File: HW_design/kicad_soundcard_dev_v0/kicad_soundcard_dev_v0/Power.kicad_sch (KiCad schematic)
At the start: 18 parts, among them J101 USB_C_Receptacle_USB2.0_16P, U101 AMS1117-3.3, U102 AMS1117-3.3

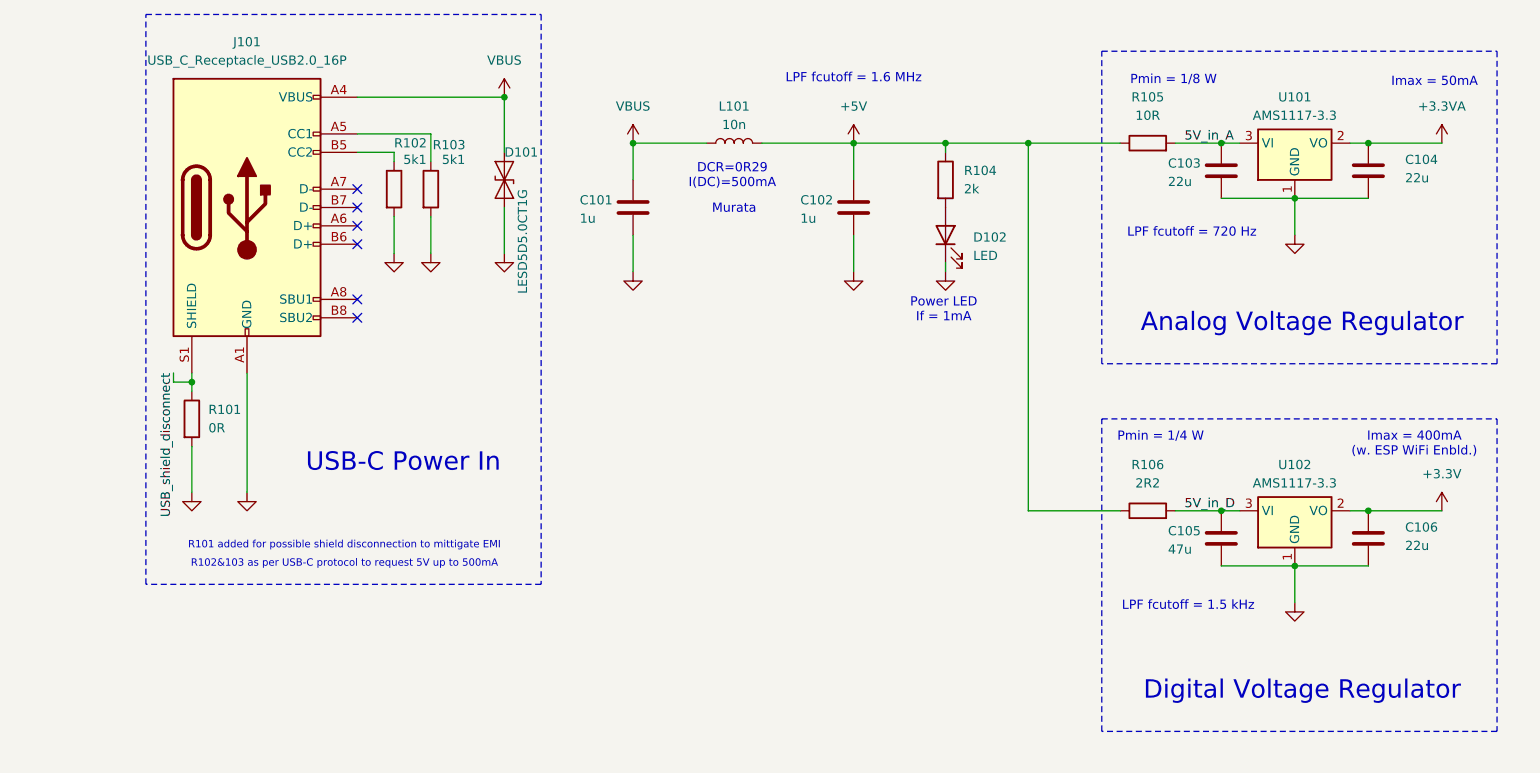
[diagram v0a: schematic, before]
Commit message: Changed Directory structure
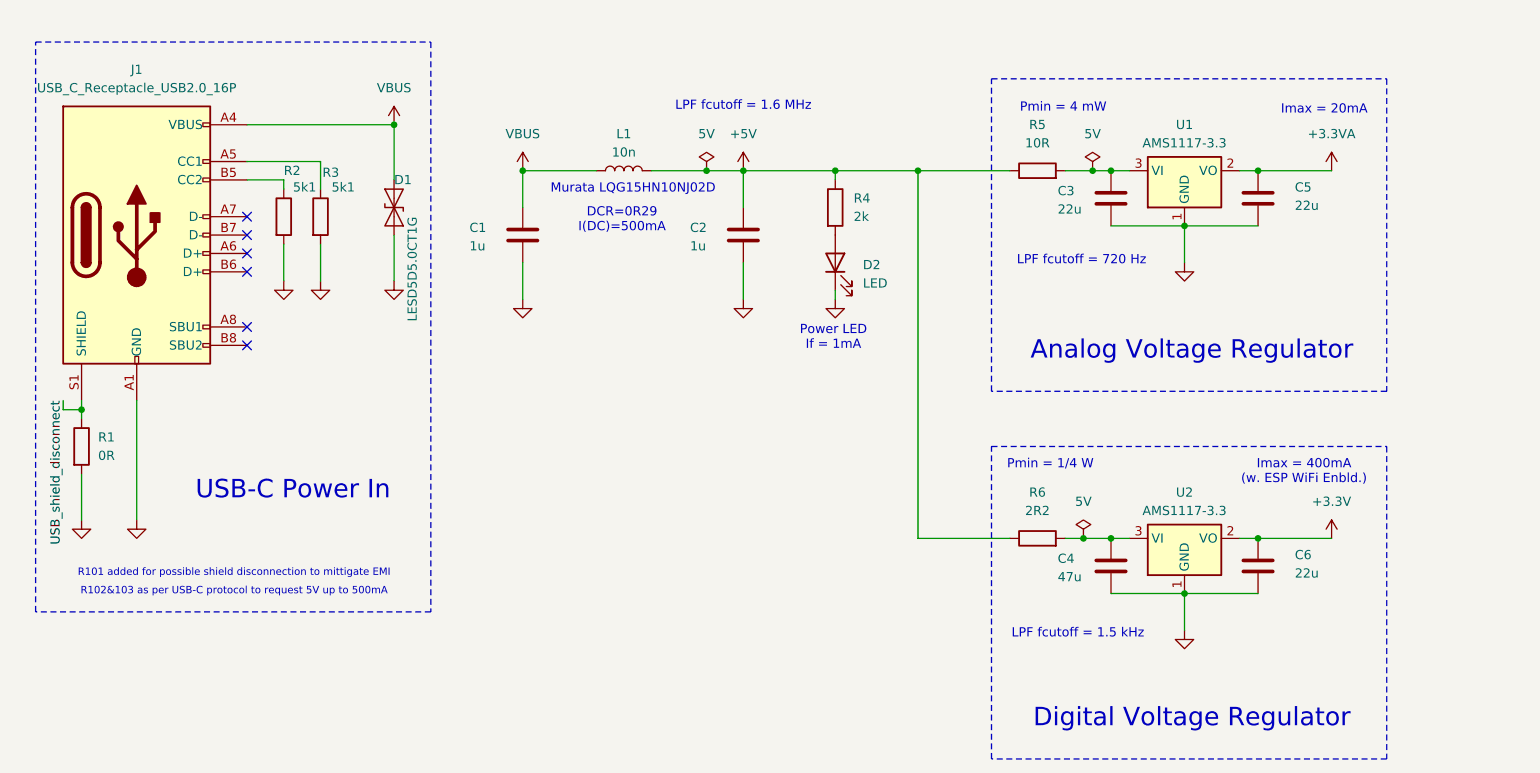
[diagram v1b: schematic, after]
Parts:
- removed C101, C102: 1u, Capacitor_SMD:C_0402_1005Metric, symbol Device:C
- removed C103, C104, C106: 22u, Capacitor_SMD:C_0603_1608Metric, symbol Device:C
- removed C105: 47u, Capacitor_SMD:C_0603_1608Metric, symbol Device:C
- removed D101: LESD5D5.0CT1G, Diode_SMD:D_SOD-523, symbol Diode:ESD9B5.0ST5G
- removed D102: LED, LED_SMD:LED_0402_1005Metric, symbol Device:LED
- removed J101: USB_C_Receptacle_USB2.0_16P, Connector_USB:USB_C_Receptacle_Palconn_UTC16-G, symbol Connector:USB_C_Receptacle_USB2.0_16P
- removed L101: 10n, Inductor_SMD:L_0402_1005Metric, symbol Device:L
- removed R101: 0R, Resistor_SMD:R_0805_2012Metric, symbol Device:R
- removed R102, R103: 5k1, Resistor_SMD:R_0402_1005Metric, symbol Device:R
- removed R104: 2k, Resistor_SMD:R_0402_1005Metric, symbol Device:R
- removed R105: 10R, Resistor_SMD:R_0805_2012Metric, symbol Device:R
- removed R106: 2R2, Resistor_SMD:R_1206_3216Metric, symbol Device:R
- removed U101, U102: AMS1117-3.3, Package_TO_SOT_SMD:SOT-223-3_TabPin2, symbol Regulator_Linear:AMS1117-3.3
- added C1, C2: 1u, Capacitor_SMD:C_0402_1005Metric, symbol Device:C
- added C3, C5, C6: 22u, Capacitor_SMD:C_0603_1608Metric, symbol Device:C
- added C4: 47u, Capacitor_SMD:C_0603_1608Metric, symbol Device:C
- added D1: LESD5D5.0CT1G, Diode_SMD:D_SOD-523, symbol Diode:ESD9B5.0ST5G
- added D2: LED, LED_SMD:LED_0402_1005Metric, symbol Device:LED
- added J1: USB_C_Receptacle_USB2.0_16P, Connector_USB:USB_C_Receptacle_Palconn_UTC16-G, symbol Connector:USB_C_Receptacle_USB2.0_16P
- added L1: 10n, Inductor_SMD:L_0402_1005Metric, symbol Device:L
- added R1: 0R, Resistor_SMD:R_0603_1608Metric, symbol Device:R
- added R2, R3: 5k1, Resistor_SMD:R_0402_1005Metric, symbol Device:R
- added R4: 2k, Resistor_SMD:R_0402_1005Metric, symbol Device:R
- added R5: 10R, Resistor_SMD:R_0603_1608Metric, symbol Device:R
- added R6: 2R2, Resistor_SMD:R_1206_3216Metric, symbol Device:R
- added U1, U2: AMS1117-3.3, Package_TO_SOT_SMD:SOT-223-3_TabPin2, symbol Regulator_Linear:AMS1117-3.3
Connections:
- net +3.3V: now also C6.1, U2.2 (VO)
- net +3.3VA: now also C5.1, U1.2 (VO)
- net +5V: now also C2.1, L1.2, R4.1, R5.1, R6.1
- net GND: now also C1.2, C2.2, C3.2, C4.2, C5.2, C6.2, D1.1 (A1), D2.1 (K), J1.A1 (GND), J1.A12 (GND), J1.B1 (GND), J1.B12 (GND), R1.2, R2.2, R3.2, U1.1 (GND), U2.1 (GND)
- net USB_shield_disconnect: now also J1.S1 (SHIELD), R1.1
- net VBUS: now also C1.1, D1.2 (A2), J1.A4 (VBUS), J1.A9 (VBUS), J1.B4 (VBUS), J1.B9 (VBUS), L1.1
- new net: D2.2 (A), R4.2
- new net: C4.1, R6.2, U2.3 (VI)
- new net: J1.B5 (CC2), R2.1
- new net: C3.1, R5.2, U1.3 (VI)
- new net: J1.A5 (CC1), R3.1
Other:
- note added: "Imax = 20mA"
- note added: "Murata LQG15HN10NJ02D"
- note added: "Pmin = 4 mW"
- note removed: "Imax = 50mA"
- note removed: "Murata"
- note removed: "Pmin = 1/8 W"
- company: (none) -> BUCHAREST APPLIED STEAM MUSEUM
- title: (none) -> BASM SOUNDCARD DEV V0

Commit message: Schematic Rev2 + PCB Initial Release
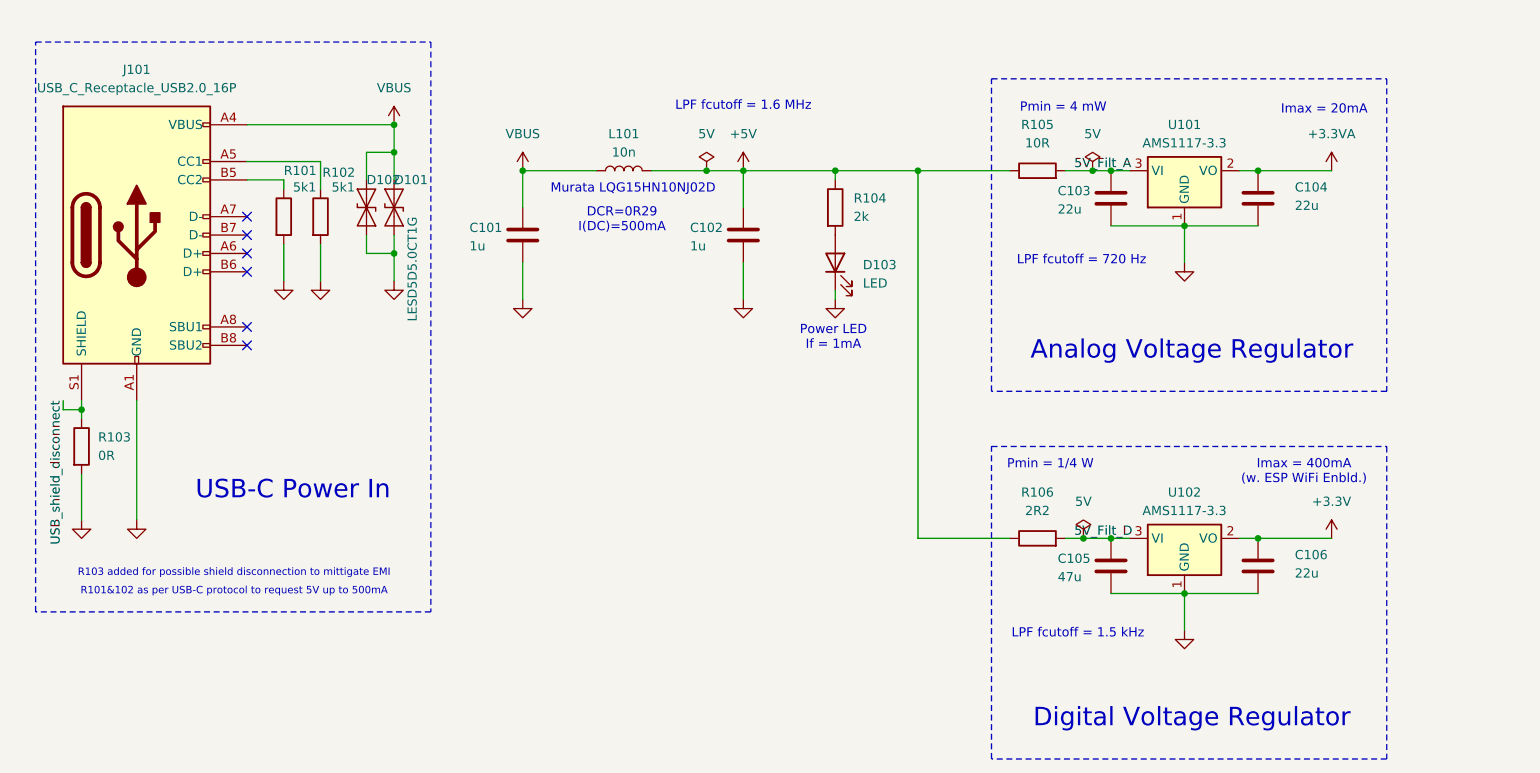
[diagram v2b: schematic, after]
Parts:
- added D102: LESD5D5.0CT1G, Diode_SMD:D_SOD-523, symbol Diode:ESD9B5.0ST5G
- J101: renamed from J1; footprint Connector_USB:USB_C_Receptacle_Palconn_UTC16-G -> Connector_USB:USB_C_Receptacle_HRO_TYPE-C-31-M-12
- renumbered C1 to C101, C2 to C102, C3 to C103, C5 to C104, C4 to C105, C6 to C106, D1 to D101, D2 to D103, L1 to L101, R2 to R101, R3 to R102, R1 to R103, R4 to R104, R5 to R105, R6 to R106, U1 to U101, U2 to U102
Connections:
- net GND: now also D102.1 (A1)
- net VBUS: now also D102.2 (A2)
- net 5V_Filt_D: now reaches C105.1, R106.2, U102.3 (VI)
- net 5V_Filt_A: now reaches C103.1, R105.2, U101.3 (VI)
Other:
- note added: "R101&102 as per USB-C protocol to request 5V up to 500mA"
- note added: "R103 added for possible shield disconnection to mittigate EMI"
- note removed: "R101 added for possible shield disconnection to mittigate EMI"
- note removed: "R102&103 as per USB-C protocol to request 5V up to 500mA"
